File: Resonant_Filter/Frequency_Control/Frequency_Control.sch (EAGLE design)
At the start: 9 parts

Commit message: Licenses
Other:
- note added: "2016xxx"
- note added: "Frequency Control Project by Cycfi Research is licensed under a Creative Commons Attribution-ShareAlike 4.0 International License. Copyright CYCFI Research Inc. 2013-2016"
- note removed: "-"
- note removed: "1"
- note removed: "2"
- note removed: "2016041"
- note removed: "3"
- note removed: "Resonant Filter Project by Cycfi Research is licensed under a Creative Commons Attribution-NonCommercial 4.0 International License. http://creativecommons.org/licenses/by-nc/4.0/ Copyright CYCFI Research Inc. 2013-2016"
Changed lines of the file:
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@@
 <setting verticaltext="up"/>
 </settings>
-<grid distance="0.025" unitdist="inch" unit="inch" style="lines" multiple="1" display="yes" altdistance="0.01" altunitdist="inch" altunit="inch"/>
+<grid distance="0.1" unitdist="inch" unit="inch" style="lines" multiple="1" display="no" altdistance="0.01" altunitdist="inch" altunit="inch"/>
 <layers>
 <layer number="1" name="Top" color="4" fill="1" visible="no" active="no"/>
@@
 <text x="177.8" y="19.05" size="2.54" layer="95">Frequency Control</text>
 <text x="252.73" y="6.985" size="2.1844" layer="95">v1.46</text>
-<text x="7.62" y="12.7" size="2.54" layer="95">Resonant Filter Project by Cycfi Research is licensed under a
-Creative Commons Attribution-NonCommercial 4.0 International License.
-http://creativecommons.org/licenses/by-nc/4.0/
+<text x="7.62" y="12.7" size="2.54" layer="95">Frequency Control Project by Cycfi Research is licensed under a
+Creative Commons Attribution-ShareAlike 4.0 International License.
 Copyright CYCFI Research Inc. 2013-2016</text>
-<text x="200.66" y="11.43" size="2.54" layer="95">2016041</text>
+<text x="200.66" y="11.43" size="2.54" layer="95">2016xxx</text>
 <wire x1="192.47528125" y1="25.047221875" x2="190.115640625" y2="25.047221875" width="0" layer="94"/>
 <wire x1="190.115640625" y1="25.047221875" x2="188.10833125" y2="25.047225" width="0" layer="94"/>
@@
 <vertex x="232.684540625" y="25.047221875"/>
 </polygon>
-<text x="103.505" y="123.825" size="1.778" layer="95">1</text>
-<text x="103.505" y="121.285" size="1.778" layer="95">2</text>
-<text x="103.505" y="118.745" size="1.778" layer="95">3</text>
-<text x="103.505" y="116.205" size="1.778" layer="95">-</text>
 </plain>
 <instances>

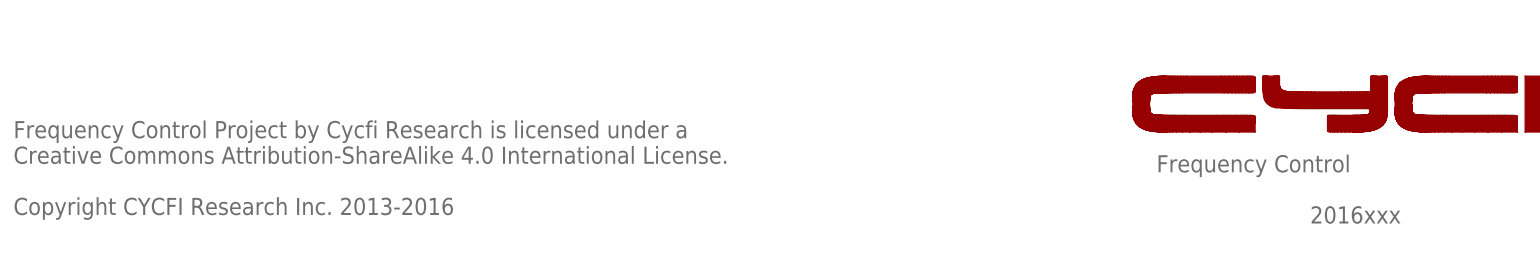
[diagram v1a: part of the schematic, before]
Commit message: *organize 5-waay switch and its configuration board(a and b) *update license date *remove red frame schem pdf files, change with black frame *update document number
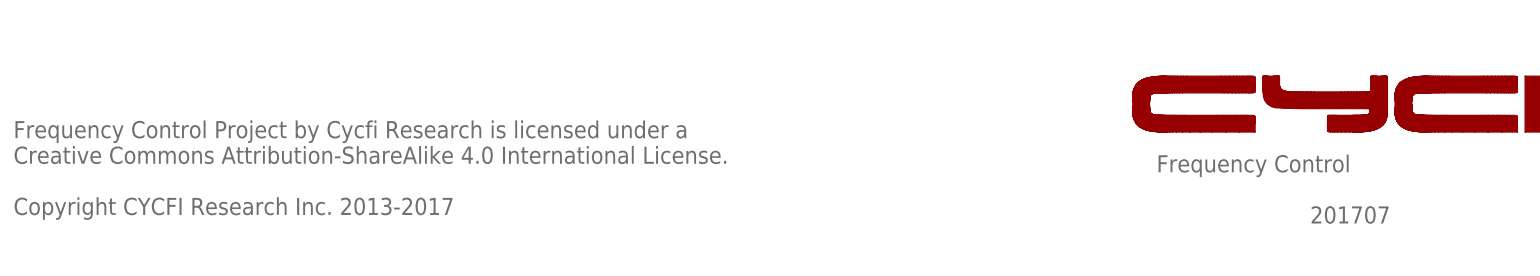
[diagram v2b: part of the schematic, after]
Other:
- note added: "201707"
- note added: "Frequency Control Project by Cycfi Research is licensed under a Creative Commons Attribution-ShareAlike 4.0 International License. Copyright CYCFI Research Inc. 2013-2017"
- note removed: "2016xxx"
- note removed: "Frequency Control Project by Cycfi Research is licensed under a Creative Commons Attribution-ShareAlike 4.0 International License. Copyright CYCFI Research Inc. 2013-2016"
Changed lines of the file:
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@@
 <text x="7.62" y="12.7" size="2.54" layer="95">Frequency Control Project by Cycfi Research is licensed under a
 Creative Commons Attribution-ShareAlike 4.0 International License.
-Copyright CYCFI Research Inc. 2013-2016</text>
-<text x="200.66" y="11.43" size="2.54" layer="95">2016xxx</text>
+Copyright CYCFI Research Inc. 2013-2017</text>
+<text x="200.66" y="11.43" size="2.54" layer="95">201707</text>
 <wire x1="192.47528125" y1="25.047221875" x2="190.115640625" y2="25.047221875" width="0" layer="94"/>
 <wire x1="190.115640625" y1="25.047221875" x2="188.10833125" y2="25.047225" width="0" layer="94"/>

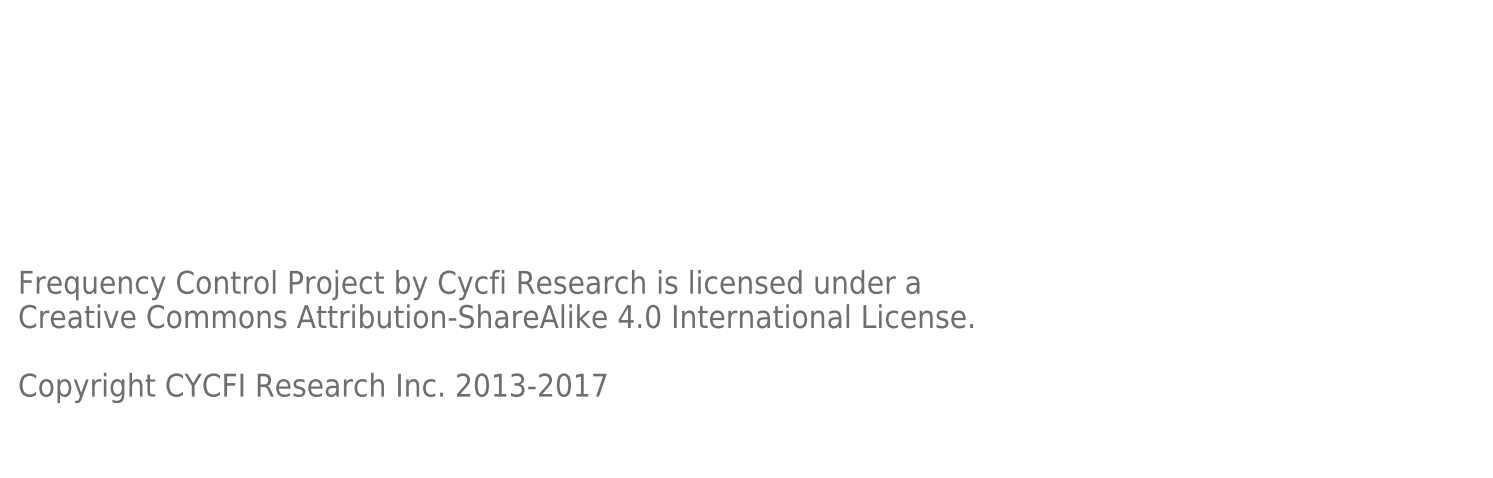
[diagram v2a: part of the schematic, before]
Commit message: Updated broken .sch files
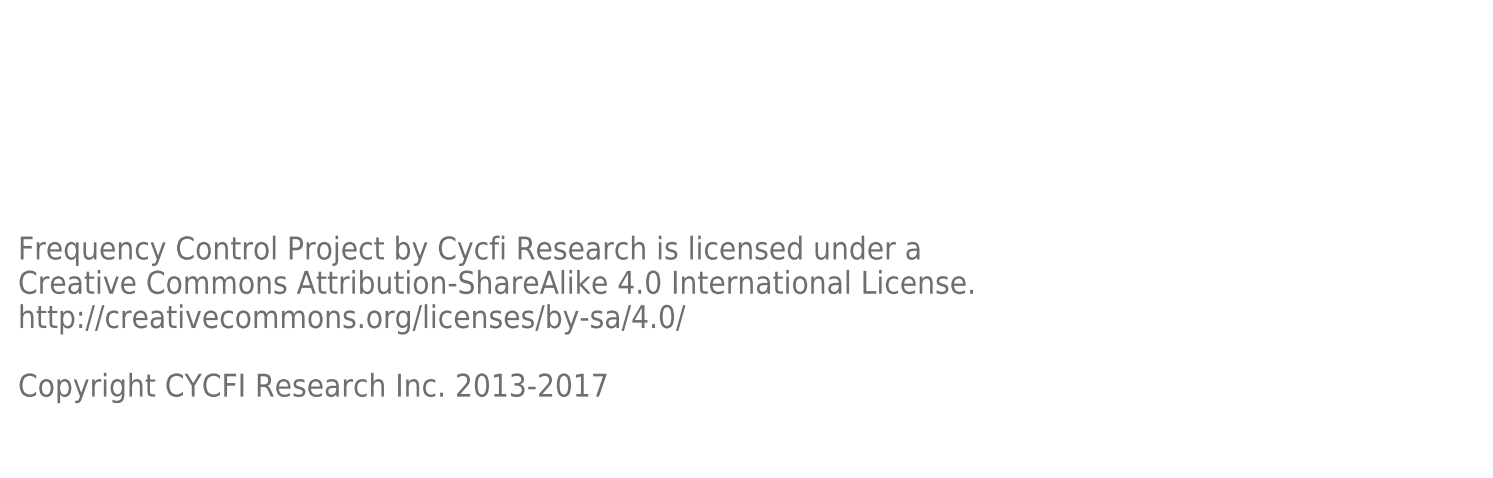
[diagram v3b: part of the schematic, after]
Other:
- note added: "Frequency Control Project by Cycfi Research is licensed under a Creative Commons Attribution-ShareAlike 4.0 International License. http://creativecommons.org/licenses/by-sa/4.0/ Copyright CYCFI Research Inc. 2013-2017"
- note removed: "Frequency Control Project by Cycfi Research is licensed under a Creative Commons Attribution-ShareAlike 4.0 International License. Copyright CYCFI Research Inc. 2013-2017"
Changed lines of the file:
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@@
 <text x="7.62" y="12.7" size="2.54" layer="95">Frequency Control Project by Cycfi Research is licensed under a
 Creative Commons Attribution-ShareAlike 4.0 International License.
+http://creativecommons.org/licenses/by-sa/4.0/
 Copyright CYCFI Research Inc. 2013-2017</text>
 <text x="200.66" y="11.43" size="2.54" layer="95">201707</text>
